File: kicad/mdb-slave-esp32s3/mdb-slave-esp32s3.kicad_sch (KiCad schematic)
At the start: 45 parts, among them J1 MDB_Connector, J2 USB_C_Receptacle_USB2.0_16P, J3 Conn_01x03_Pin, J8 Conn_01x04_Pin, Q7 MMBT3904, SW1 SW_Push, U1 TLP785, U3 ESP32-S3FH4R2, U4 TLP785, U5 LM2594HVM-3.3, Y1 Crystal_GND24

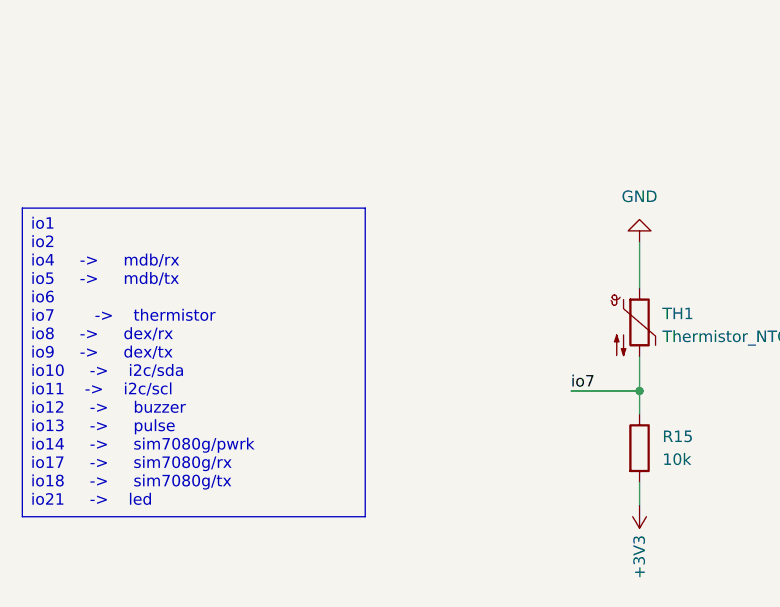
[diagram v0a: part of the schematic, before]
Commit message: feat(kicad-slave): add 2x11 extension pin header (J4) for add-on modules
Reproduces the historical breakout header (commit c5da6d6) on the WiFi
ESP32-S3 slave so extension modules can be plugged on top. J4 =
Conn_02x11_Odd_Even with the exact historical pin->net mapping: UART0
(u0txd/u0rxd) + all 16 GPIOs (io1..io21) + 3V3 + VIN + 3x GND.

- Schematic: J4 + 22 net labels, pinout verified pin-by-pin vs c5da6d6
- PCB: left Edge.Cuts extended 9.5mm (board 48.5x40mm); J4 placed in the
  new strip, all 22 pads net-assigned, clears the H1 mounting hole
- schematic<->PCB net-consistent (22/22); DRC adds zero new violations
  vs baseline (and removed 4 pre-existing copper_edge_clearance errors)
- J3/J8/SW1/H1 and all other parts unchanged
- Routing pending (traces not yet drawn)

Spec: docs/superpowers/specs/2026-06-08-slave-extension-header-design.md

Co-Authored-By: Claude Opus 4.8 <noreply@anthropic.com>
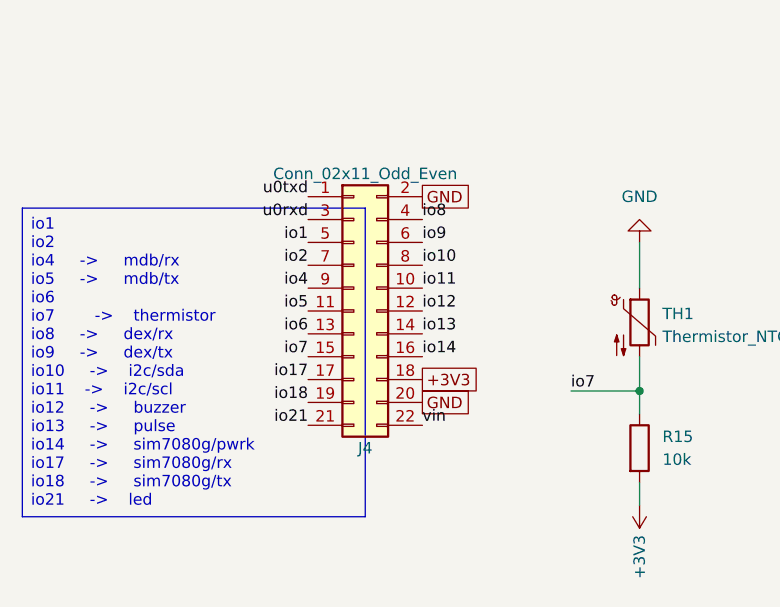
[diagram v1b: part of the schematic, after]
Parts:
- added J4: Conn_02x11_Odd_Even, Connector_PinHeader_2.54mm:PinHeader_2x11_P2.54mm_Vertical, symbol Connector_Generic:Conn_02x11_Odd_Even
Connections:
- net +3V3: now also J4.18 (Pin_18)
- net GND: now also J4.2 (Pin_2), J4.20 (Pin_20)
- net io1: now also J4.5 (Pin_5)
- net io10: now also J4.8 (Pin_8)
- net io11: now also J4.10 (Pin_10)
- net io12: now also J4.12 (Pin_12)
- net io13: now also J4.14 (Pin_14)
- net io14: now also J4.16 (Pin_16)
- net io17: now also J4.17 (Pin_17)
- net io18: now also J4.19 (Pin_19)
- net io2: now also J4.7 (Pin_7)
- net io21: now also J4.21 (Pin_21)
- net io4: now also J4.9 (Pin_9)
- net io5: now also J4.11 (Pin_11)
- net io6: now also J4.13 (Pin_13)
- net io7: now also J4.15 (Pin_15)
- net io8: now also J4.4 (Pin_4)
- net io9: now also J4.6 (Pin_6)
- net u0rxd: now also J4.3 (Pin_3)
- net u0txd: now also J4.1 (Pin_1)
- net vin: now also J4.22 (Pin_22)
